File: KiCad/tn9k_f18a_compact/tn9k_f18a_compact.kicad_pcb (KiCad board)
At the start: 2 copper layers, 32 x 94.9 mm, 27 parts, among them J2 VGA, J3 Tang Nano 9k, J4 TN9k/2, J5 VGA, J6 VGA, U1 1G08, U4 74LCX16245

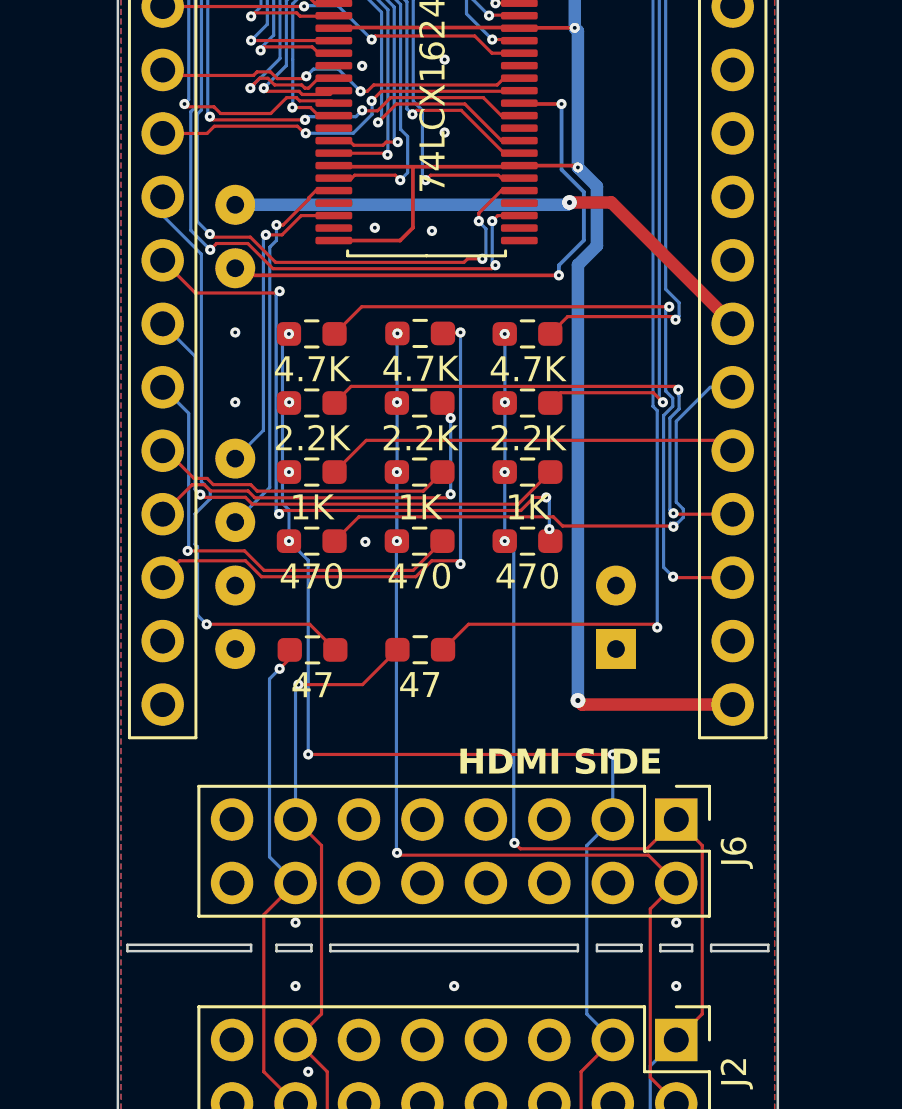
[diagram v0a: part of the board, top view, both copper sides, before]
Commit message: Add diode to prevent host being powered from TN9k
HDMI has a +5V supply line that could halfway power up the TI-99/4A
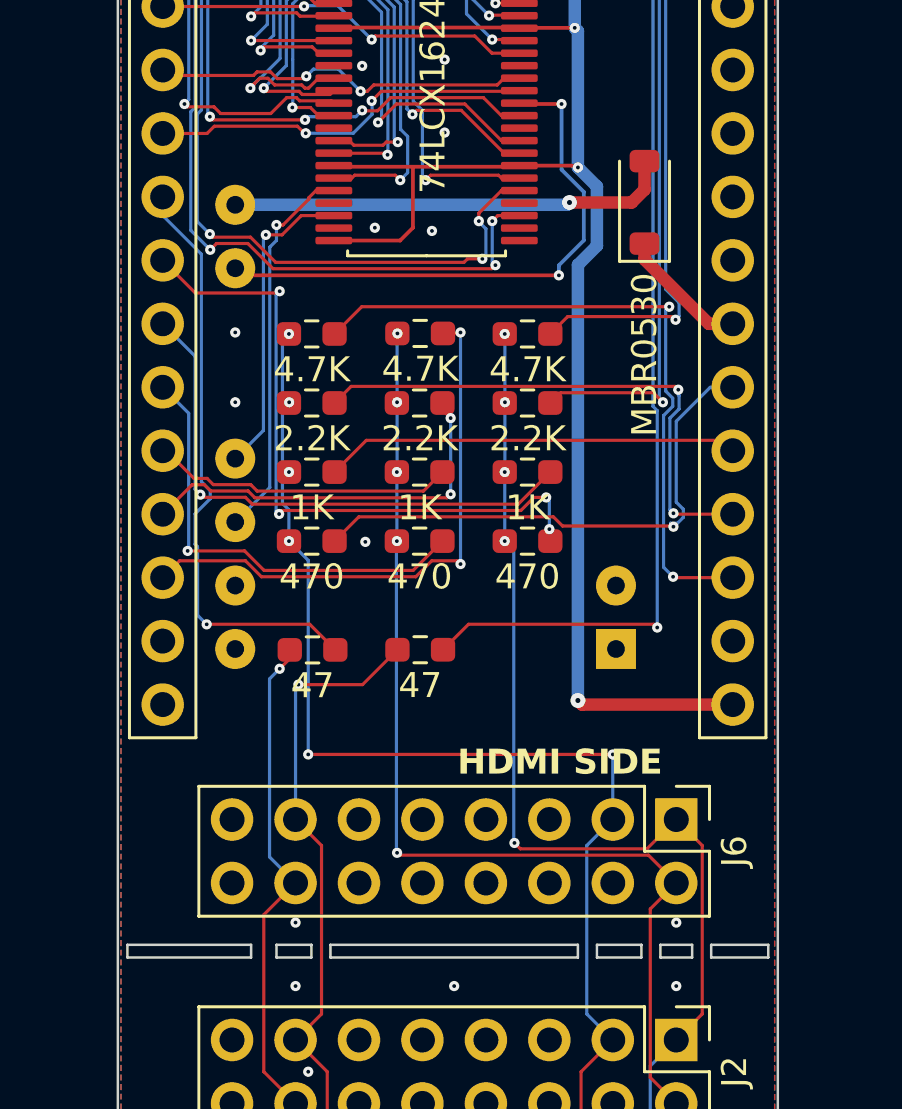
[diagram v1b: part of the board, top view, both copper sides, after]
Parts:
- added D1: MBR0530, Diode_SMD:D_SOD-123, F.Cu at (123.8, 98.4)
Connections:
- J4 pad 18: +5V -> Net-(D1-K)
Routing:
- net Net-(D1-K): track 0.00 -> 5.23 mm
- net +5V: track 22.0 -> 17.8 mm
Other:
- outline, holes or cut-outs redrawn
